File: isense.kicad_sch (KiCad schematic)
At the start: 29 parts, among them U1 MAX4073T, U2 OPA551U, U3 TLV9301xDBV, U4 OPA551U, U5 TLV9301xDBV

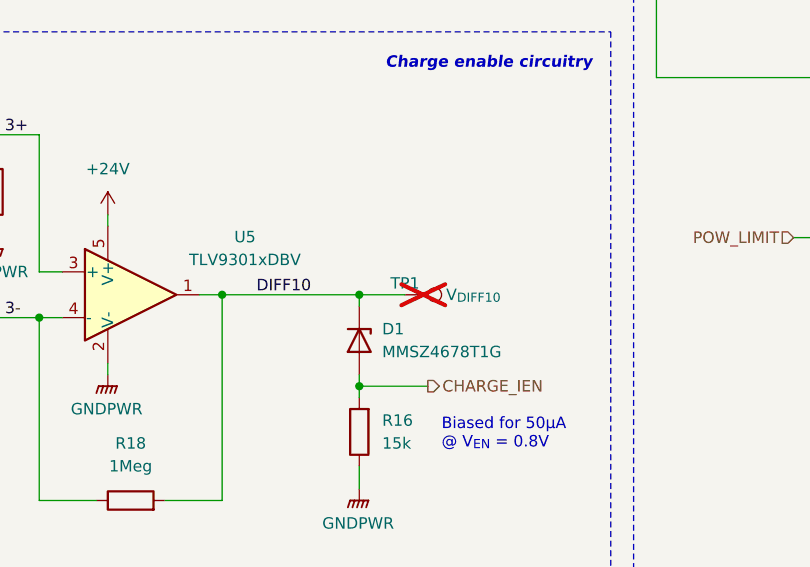
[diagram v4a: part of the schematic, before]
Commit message: Begin layout
Completed ideal diode layout
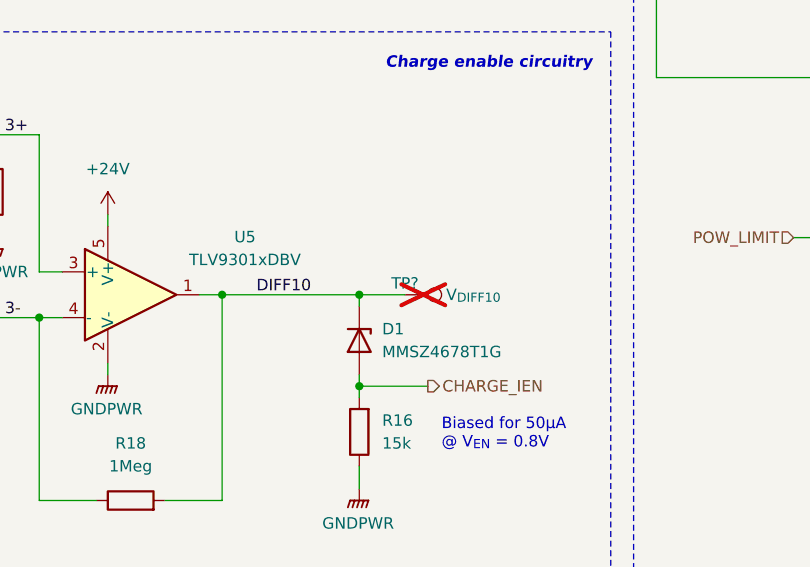
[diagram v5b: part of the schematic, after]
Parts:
- renumbered TP1 to TP?
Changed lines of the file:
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@@
 		(dnp no)
 		(fields_autoplaced yes)
-		(property "Reference" "#PWR040"
+		(property "Reference" "#PWR019"
 			(at 96.52 52.07 0)
 			(effects
@@
 		(dnp no)
 		(fields_autoplaced yes)
-		(property "Reference" "#PWR054"
+		(property "Reference" "#PWR033"
 			(at 158.75 140.97 0)
 			(effects
@@
 		(on_board yes)
 		(dnp yes)
-		(property "Reference" "TP1"
+		(property "Reference" "TP?"
 			(at 163.83 113.03 90)
 			(effects
@@
 		)
 		(instances
+			(project "SupercapManager"
+				(path "/6197145b-e7d4-44cc-9d90-537b6501bf60/9739d4cc-938e-4869-b5d8-561f0e1056cb"
+					(reference "TP?")
+					(unit 1)
+				)
+			)
 			(project "Rev 1B"
 				(path "/e5f99deb-ef42-4c5f-b80a-388477910e20/271408e9-0010-4c59-8c9c-96a1532c4998"
@@
 		(dnp no)
 		(fields_autoplaced yes)
-		(property "Reference" "#PWR043"
+		(property "Reference" "#PWR022"
 			(at 132.08 69.85 0)
 			(effects
@@
 		(dnp no)
 		(fields_autoplaced yes)
-		(property "Reference" "#PWR050"
+		(property "Reference" "#PWR029"
 			(at 118.11 113.03 0)
 			(effects
@@
 		(dnp no)
 		(fields_autoplaced yes)
-		(property "Reference" "#PWR048"
+		(property "Reference" "#PWR027"
 			(at 223.52 106.68 0)
 			(effects
@@
 		(dnp no)
 		(fields_autoplaced yes)
-		(property "Reference" "#PWR039"
+		(property "Reference" "#PWR018"
 			(at 54.61 52.07 0)
 			(effects
@@
 		(dnp no)
 		(fields_autoplaced yes)
-		(property "Reference" "#PWR044"
+		(property "Reference" "#PWR023"
 			(at 181.61 71.12 0)
 			(effects
@@
 		(dnp no)
 		(fields_autoplaced yes)
-		(property "Reference" "#PWR038"
+		(property "Reference" "#PWR017"
 			(at 223.52 50.8 0)
 			(effects
@@
 		(dnp no)
 		(fields_autoplaced yes)
-		(property "Reference" "#PWR042"
+		(property "Reference" "#PWR021"
 			(at 181.61 53.34 0)
 			(effects
@@
 		(dnp no)
 		(fields_autoplaced yes)
-		(property "Reference" "#PWR041"
+		(property "Reference" "#PWR020"
 			(at 132.08 53.34 0)
 			(effects
@@
 		(dnp no)
 		(fields_autoplaced yes)
-		(property "Reference" "#PWR049"
+		(property "Reference" "#PWR028"
 			(at 130.81 109.22 0)
 			(effects
@@
 		(dnp no)
 		(fields_autoplaced yes)
-		(property "Reference" "#PWR055"
+		(property "Reference" "#PWR034"
 			(at 243.84 143.51 0)
 			(effects
@@
 		(dnp no)
 		(fields_autoplaced yes)
-		(property "Reference" "#PWR046"
+		(property "Reference" "#PWR025"
 			(at 243.84 87.63 0)
 			(effects
@@
 		(dnp no)
 		(fields_autoplaced yes)
-		(property "Reference" "#PWR037"
+		(property "Reference" "#PWR016"
 			(at 243.84 44.45 0)
 			(effects
@@
 		(dnp no)
 		(fields_autoplaced yes)
-		(property "Reference" "#PWR051"
+		(property "Reference" "#PWR030"
 			(at 130.81 128.27 0)
 			(effects
@@
 		(dnp no)
 		(fields_autoplaced yes)
-		(property "Reference" "#PWR047"
+		(property "Reference" "#PWR026"
 			(at 243.84 100.33 0)
 			(effects
@@
 		(dnp no)
 		(fields_autoplaced yes)
-		(property "Reference" "#PWR053"
+		(property "Reference" "#PWR032"
 			(at 93.98 140.97 0)
 			(effects
@@
 		(dnp no)
 		(fields_autoplaced yes)
-		(property "Reference" "#PWR045"
+		(property "Reference" "#PWR024"
 			(at 96.52 71.12 0)
 			(effects
@@
 		(dnp no)
 		(fields_autoplaced yes)
-		(property "Reference" "#PWR052"
+		(property "Reference" "#PWR031"
 			(at 93.98 129.54 0)
 			(effects

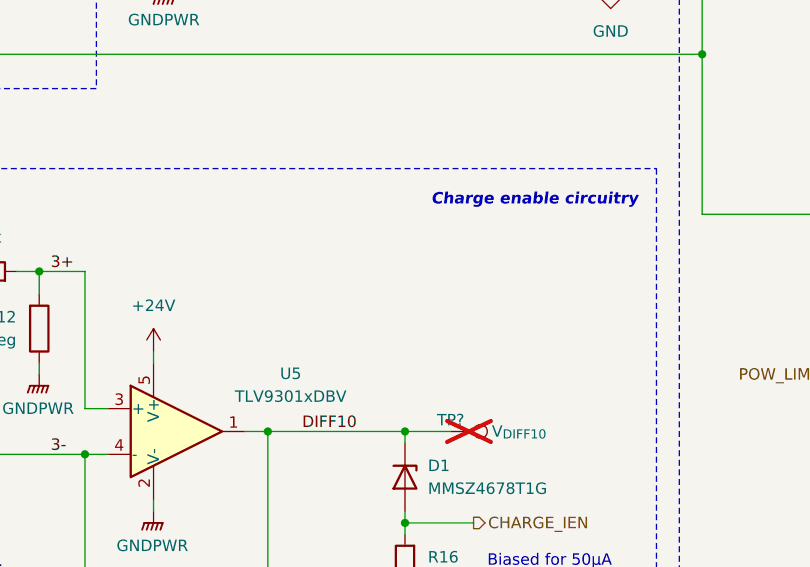
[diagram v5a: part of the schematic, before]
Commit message: Add documentation to isense sheet
Also fiddle with simulations
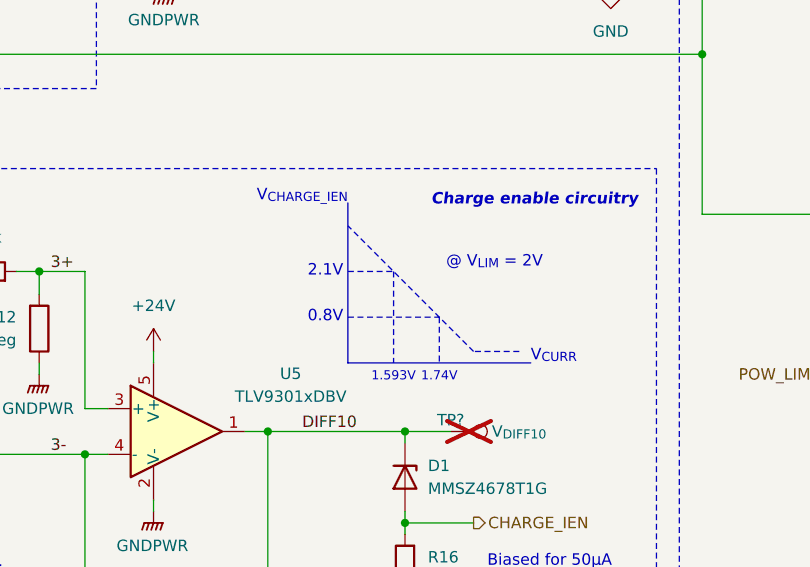
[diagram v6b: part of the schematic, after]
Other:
- note added: "0.8V"
- note added: "1.593V"
- note added: "1.74V"
- note added: "2.1V"
- note added: "@ V_{LIM} = 2V"
- note added: "V_{CHARGE_IEN}"
- note added: "V_{CURR}"
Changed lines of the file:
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@@
+		)
+	)
+	(text "1.593V"
+		(exclude_from_sim no)
+		(at 157.48 107.696 0)
+		(effects
+			(font
+				(size 1.016 1.016)
+			)
+			(justify top)
 		)
 	)
@@
 		)
 	)
+	(text "0.8V"
+		(exclude_from_sim no)
+		(at 151.892 101.6 0)
+		(effects
+			(font
+				(size 1.27 1.27)
+			)
+			(justify right)
+		)
+	)
+	(text "1.74V"
+		(exclude_from_sim no)
+		(at 162.56 107.696 0)
+		(effects
+			(font
+				(size 1.016 1.016)
+			)
+			(justify top)
+		)
+	)
 	(text "20V/V amplification\n= ~2V of swing (0-120W)"
 		(exclude_from_sim no)
@@
 		)
 	)
+	(text "V_{CHARGE_IEN}"
+		(exclude_from_sim no)
+		(at 152.4 88.9 0)
+		(effects
+			(font
+				(size 1.27 1.27)
+			)
+			(justify right bottom)
+		)
+	)
+	(text "V_{CURR}"
+		(exclude_from_sim no)
+		(at 172.72 106.68 0)
+		(effects
+			(font
+				(size 1.27 1.27)
+			)
+			(justify left bottom)
+		)
+	)
 	(text "R_{S} chosen such that the max\ncurrent of 5A (@120W) is 100mV"
 		(exclude_from_sim no)
@@
 			)
 			(justify left top)
+		)
+	)
+	(text "2.1V"
+		(exclude_from_sim no)
+		(at 151.892 96.52 0)
+		(effects
+			(font
+				(size 1.27 1.27)
+			)
+			(justify right)
 		)
 	)
@@
 		)
 	)
+	(text "@ V_{LIM} = 2V"
+		(exclude_from_sim no)
+		(at 163.322 96.266 0)
+		(effects
+			(font
+				(size 1.27 1.27)
+			)
+			(justify left bottom)
+		)
+	)
 	(junction
 		(at 223.52 90.17)
@@
 	(polyline
 		(pts
+			(xy 166.37 105.41) (xy 152.4 91.44)
+		)
+		(stroke
+			(width 0)
+			(type dash)
+		)
+	)
+	(polyline
+		(pts
 			(xy 86.36 16.51) (xy 86.36 76.2)
 		)
@@
 		)
 	)
+	(polyline
+		(pts
+			(xy 157.48 96.52) (xy 157.48 106.68)
+		)
+		(stroke
+			(width 0)
+			(type dot)
+		)
+	)
 	(wire
 		(pts
@@
 		)
 	)
+	(polyline
+		(pts
+			(xy 152.4 88.9) (xy 152.4 106.68)
+		)
+		(stroke
+			(width 0)
+			(type default)
+		)
+	)
 	(wire
 		(pts
@@
 		)
 	)
+	(polyline
+		(pts
+			(xy 152.4 101.6) (xy 162.56 101.6)
+		)
+		(stroke
+			(width 0)
+			(type dot)
+		)
+	)
 	(wire
 		(pts
@@
 		)
 	)
+	(polyline
+		(pts
+			(xy 152.4 106.68) (xy 172.72 106.68)
+		)
+		(stroke
+			(width 0)
+			(type default)
+		)
+	)
 	(wire
 		(pts
@@
 		)
 	)
+	(polyline
+		(pts
+			(xy 162.56 101.6) (xy 162.56 106.68)
+		)
+		(stroke
+			(width 0)
+			(type dot)
+		)
+	)
 	(wire
 		(pts
@@
 		)
 	)
+	(polyline
+		(pts
+			(xy 171.45 105.41) (xy 166.37 105.41)
+		)
+		(stroke
+			(width 0)
+			(type dash)
+		)
+	)
 	(wire
 		(pts
@@
 		)
 	)
+	(polyline
+		(pts
+			(xy 152.4 96.52) (xy 157.48 96.52)
+		)
+		(stroke
+			(width 0)
+			(type dot)
+		)
+	)

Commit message: Completed preliminary layout
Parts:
- gave numbers to parts that had none: 1
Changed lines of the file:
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@@
 		(dnp no)
 		(fields_autoplaced yes)
-		(property "Reference" "#PWR019"
+		(property "Reference" "#PWR040"
 			(at 96.52 52.07 0)
 			(effects
@@
 		(dnp no)
 		(fields_autoplaced yes)
-		(property "Reference" "#PWR033"
+		(property "Reference" "#PWR054"
 			(at 158.75 140.97 0)
 			(effects
@@
 		(on_board yes)
 		(dnp yes)
-		(property "Reference" "TP?"
+		(property "Reference" "TP1"
 			(at 163.83 113.03 90)
 			(effects
@@
 		(dnp no)
 		(fields_autoplaced yes)
-		(property "Reference" "#PWR022"
+		(property "Reference" "#PWR043"
 			(at 132.08 69.85 0)
 			(effects
@@
 		(dnp no)
 		(fields_autoplaced yes)
-		(property "Reference" "#PWR029"
+		(property "Reference" "#PWR050"
 			(at 118.11 113.03 0)
 			(effects
@@
 		(dnp no)
 		(fields_autoplaced yes)
-		(property "Reference" "#PWR027"
+		(property "Reference" "#PWR048"
 			(at 223.52 106.68 0)
 			(effects
@@
 		(dnp no)
 		(fields_autoplaced yes)
-		(property "Reference" "#PWR018"
+		(property "Reference" "#PWR039"
 			(at 54.61 52.07 0)
 			(effects
@@
 		(dnp no)
 		(fields_autoplaced yes)
-		(property "Reference" "#PWR023"
+		(property "Reference" "#PWR044"
 			(at 181.61 71.12 0)
 			(effects
@@
 		(dnp no)
 		(fields_autoplaced yes)
-		(property "Reference" "#PWR017"
+		(property "Reference" "#PWR038"
 			(at 223.52 50.8 0)
 			(effects
@@
 		(dnp no)
 		(fields_autoplaced yes)
-		(property "Reference" "#PWR021"
+		(property "Reference" "#PWR042"
 			(at 181.61 53.34 0)
 			(effects
@@
 		(dnp no)
 		(fields_autoplaced yes)
-		(property "Reference" "#PWR020"
+		(property "Reference" "#PWR041"
 			(at 132.08 53.34 0)
 			(effects
@@
 		(dnp no)
 		(fields_autoplaced yes)
-		(property "Reference" "#PWR028"
+		(property "Reference" "#PWR049"
 			(at 130.81 109.22 0)
 			(effects
@@
 		(dnp no)
 		(fields_autoplaced yes)
-		(property "Reference" "#PWR034"
+		(property "Reference" "#PWR055"
 			(at 243.84 143.51 0)
 			(effects
@@
 		(dnp no)
 		(fields_autoplaced yes)
-		(property "Reference" "#PWR025"
+		(property "Reference" "#PWR046"
 			(at 243.84 87.63 0)
 			(effects
@@
 		(dnp no)
 		(fields_autoplaced yes)
-		(property "Reference" "#PWR016"
+		(property "Reference" "#PWR037"
 			(at 243.84 44.45 0)
 			(effects
@@
 		(dnp no)
 		(fields_autoplaced yes)
-		(property "Reference" "#PWR030"
+		(property "Reference" "#PWR051"
 			(at 130.81 128.27 0)
 			(effects
@@
 		(dnp no)
 		(fields_autoplaced yes)
-		(property "Reference" "#PWR026"
+		(property "Reference" "#PWR047"
 			(at 243.84 100.33 0)
 			(effects
@@
 		(dnp no)
 		(fields_autoplaced yes)
-		(property "Reference" "#PWR032"
+		(property "Reference" "#PWR053"
 			(at 93.98 140.97 0)
 			(effects
@@
 		(dnp no)
 		(fields_autoplaced yes)
-		(property "Reference" "#PWR024"
+		(property "Reference" "#PWR045"
 			(at 96.52 71.12 0)
 			(effects
@@
 		(dnp no)
 		(fields_autoplaced yes)
-		(property "Reference" "#PWR031"
+		(property "Reference" "#PWR052"
 			(at 93.98 129.54 0)
 			(effects

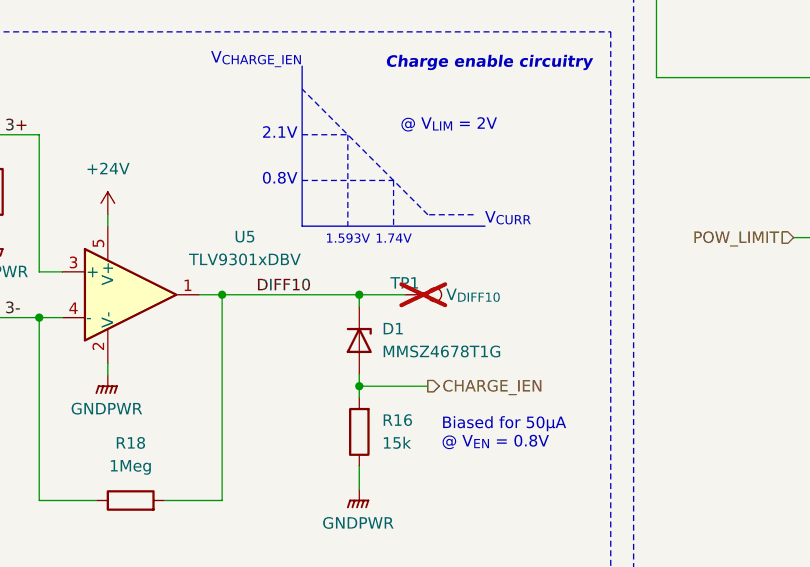
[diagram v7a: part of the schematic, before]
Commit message: Placed footprints for boost stage 1 layout
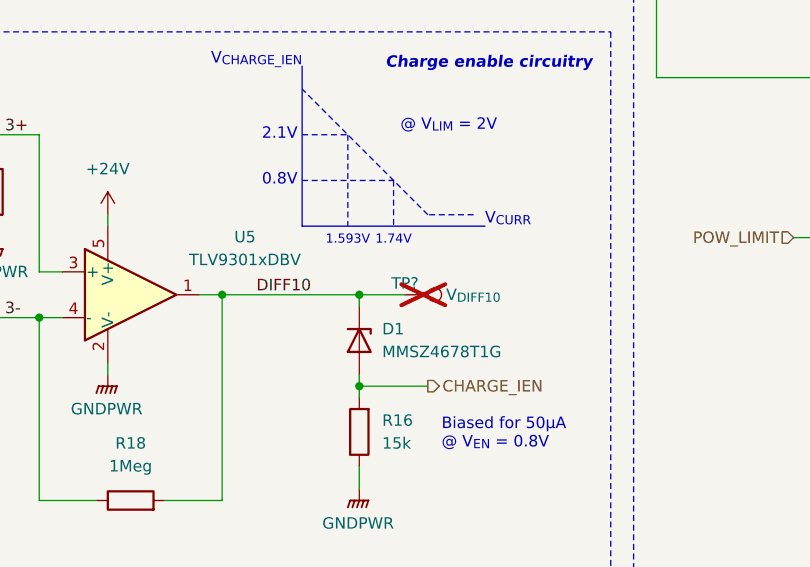
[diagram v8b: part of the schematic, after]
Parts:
- renumbered TP1 to TP?
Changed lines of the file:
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@@
 		(dnp no)
 		(fields_autoplaced yes)
-		(property "Reference" "#PWR040"
+		(property "Reference" "#PWR019"
 			(at 96.52 52.07 0)
 			(effects
@@
 		(dnp no)
 		(fields_autoplaced yes)
-		(property "Reference" "#PWR054"
+		(property "Reference" "#PWR033"
 			(at 158.75 140.97 0)
 			(effects
@@
 		(on_board yes)
 		(dnp yes)
-		(property "Reference" "TP1"
+		(property "Reference" "TP?"
 			(at 163.83 113.03 90)
 			(effects
@@
 		(dnp no)
 		(fields_autoplaced yes)
-		(property "Reference" "#PWR043"
+		(property "Reference" "#PWR022"
 			(at 132.08 69.85 0)
 			(effects
@@
 		(dnp no)
 		(fields_autoplaced yes)
-		(property "Reference" "#PWR050"
+		(property "Reference" "#PWR029"
 			(at 118.11 113.03 0)
 			(effects
@@
 		(dnp no)
 		(fields_autoplaced yes)
-		(property "Reference" "#PWR048"
+		(property "Reference" "#PWR027"
 			(at 223.52 106.68 0)
 			(effects
@@
 		(dnp no)
 		(fields_autoplaced yes)
-		(property "Reference" "#PWR039"
+		(property "Reference" "#PWR018"
 			(at 54.61 52.07 0)
 			(effects
@@
 		(dnp no)
 		(fields_autoplaced yes)
-		(property "Reference" "#PWR044"
+		(property "Reference" "#PWR023"
 			(at 181.61 71.12 0)
 			(effects
@@
 		(dnp no)
 		(fields_autoplaced yes)
-		(property "Reference" "#PWR038"
+		(property "Reference" "#PWR017"
 			(at 223.52 50.8 0)
 			(effects
@@
 		(dnp no)
 		(fields_autoplaced yes)
-		(property "Reference" "#PWR042"
+		(property "Reference" "#PWR021"
 			(at 181.61 53.34 0)
 			(effects
@@
 		(dnp no)
 		(fields_autoplaced yes)
-		(property "Reference" "#PWR041"
+		(property "Reference" "#PWR020"
 			(at 132.08 53.34 0)
 			(effects
@@
 		(dnp no)
 		(fields_autoplaced yes)
-		(property "Reference" "#PWR049"
+		(property "Reference" "#PWR028"
 			(at 130.81 109.22 0)
 			(effects
@@
 		(dnp no)
 		(fields_autoplaced yes)
-		(property "Reference" "#PWR055"
+		(property "Reference" "#PWR034"
 			(at 243.84 143.51 0)
 			(effects
@@
 		(dnp no)
 		(fields_autoplaced yes)
-		(property "Reference" "#PWR046"
+		(property "Reference" "#PWR025"
 			(at 243.84 87.63 0)
 			(effects
@@
 		(dnp no)
 		(fields_autoplaced yes)
-		(property "Reference" "#PWR037"
+		(property "Reference" "#PWR016"
 			(at 243.84 44.45 0)
 			(effects
@@
 		(dnp no)
 		(fields_autoplaced yes)
-		(property "Reference" "#PWR051"
+		(property "Reference" "#PWR030"
 			(at 130.81 128.27 0)
 			(effects
@@
 		(dnp no)
 		(fields_autoplaced yes)
-		(property "Reference" "#PWR047"
+		(property "Reference" "#PWR026"
 			(at 243.84 100.33 0)
 			(effects
@@
 		(dnp no)
 		(fields_autoplaced yes)
-		(property "Reference" "#PWR053"
+		(property "Reference" "#PWR032"
 			(at 93.98 140.97 0)
 			(effects
@@
 		(dnp no)
 		(fields_autoplaced yes)
-		(property "Reference" "#PWR045"
+		(property "Reference" "#PWR024"
 			(at 96.52 71.12 0)
 			(effects
@@
 		(dnp no)
 		(fields_autoplaced yes)
-		(property "Reference" "#PWR052"
+		(property "Reference" "#PWR031"
 			(at 93.98 129.54 0)
 			(effects
